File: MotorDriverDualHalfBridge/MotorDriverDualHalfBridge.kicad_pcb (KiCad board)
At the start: 2 copper layers, 41 parts, among them J1 Battery Terminal +, J2 Battery Terminal -, J3 Motor Battery Connection, J4 Motor Load Connection, J5 Conn_01x02_Male, J6 Conn_01x02_Male, K1 G8PM, Q1 IAUA250N04S6N005, Q2 IAUA250N04S6N005, Q3 Q_NMOS_DGS, U1 2ED21824S06J, U2 TLI4871

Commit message: PCB V0.1
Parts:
- added C14: 100uF, Capacitor_SMD:CP_Elec_10x14.3, F.Cu at (171.0, 76.2)
- added C16: 100uF, Capacitor_SMD:CP_Elec_6.3x5.4_Nichicon, F.Cu at (190.1, 94.7)
- added C17: 100uF, Capacitor_SMD:CP_Elec_6.3x5.4_Nichicon, F.Cu at (182.8, 94.7)
- added C18: 100uF, Capacitor_SMD:CP_Elec_6.3x5.4_Nichicon, F.Cu at (175.6, 94.7)
- added C19: 100uF, Capacitor_SMD:CP_Elec_6.3x5.4_Nichicon, F.Cu at (118.2, 100.6)
- added C20: 100uF, Capacitor_SMD:CP_Elec_6.3x5.4_Nichicon, F.Cu at (118.3, 114.4)
- added HS1: Heatsink_Pad, Library:HSB25-282810, F.Cu at (155.3, 105.5)
- added J10: RJ45_LED_Shielded, Connector_RJ:RJ45_Amphenol_RJHSE538X, F.Cu at (113.6, 87.4)
- added J7: Conn_01x06_Pin, Connector_PinHeader_1.27mm:PinHeader_1x06_P1.27mm_Vertical, F.Cu at (112.6, 72.3)
- added NT1: NetTie_2, NetTie:NetTie-2_SMD_Pad2.0mm, F.Cu at (165.8, 62.2)
- C10, C11, C12, R6, R7: moved to B.Cu
- C13, C6: footprint Capacitor_SMD:CP_Elec_5x4.4 -> Capacitor_SMD:CP_Elec_10x14.3
- C4, R4: moved to F.Cu
- F1: footprint Fuse:Fuseholder_Clip-5x20mm_Bel_FC-203-22_Lateral_P17.80x5.00mm_D1.17mm_Horizontal -> Fuse:Fuseholder_Blade_Mini_Keystone_3568
- J5, J6: value Conn_01x02_Male -> Conn_01x04; footprint Connector_PinHeader_1.27mm:PinHeader_1x02_P1.27mm_Vertical -> Connector_JST:JST_EH_B4B-EH-A_1x04_P2.50mm_Vertical
- Q1, Q2: footprint IFX-PG-HSOF-5-1-V:IFX-PG-HSOF-5-1-V -> Library:IAUA250N04S6N005AUMA1
- moved J2 144.0 mm to (162.6, 56.8)
- moved R10 120.3 mm to (107.3, 65.5), turned to 90 degrees
- moved R9 120.0 mm to (109.0, 65.5), turned to -90 degrees
- moved C6 116.1 mm to (126.5, 53.8), turned to 90 degrees
- moved C12 114.8 mm to (109.2, 69.3), turned to 90 degrees
- moved J1 114.4 mm to (142.6, 56.8)
- moved C9 113.7 mm to (112.2, 65.5), turned to 90 degrees
- moved C11 113.3 mm to (107.7, 69.3), turned to 90 degrees
- moved C8 112.3 mm to (110.5, 65.5), turned to 90 degrees
- moved C10 111.9 mm to (106.0, 69.3), turned to 90 degrees
- moved R7 109.8 mm to (112.5, 69.3), turned to -90 degrees
- moved R6 108.3 mm to (110.8, 69.3), turned to -90 degrees
- moved F1 105.4 mm to (137.9, 48.8)
- moved U2 104.5 mm to (127.0, 67.3)
- moved C7 101.8 mm to (124.0, 73.3), turned to 0 degrees
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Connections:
- net Net-(Q1-Pad5) renamed /V_{GH}
- net Net-(Q2-Pad5) renamed /V_{GL}
- C5 pad 2: GND -> GNDPWR
- J5 pad 1: H_{IN} -> +3.3V
- J5 pad 2: L_{IN} -> +3.3V
- J6 pad 1: VCC -> +12V
- J6 pad 2: GND -> +12V
- Q2 pad 1: GND -> GNDPWR
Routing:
- net OCD_{1}: track 0.00 -> 106.4 mm, vias 0 -> 1
- net V_{REF}: track 0.00 -> 59.8 mm
- net OCD_{2}: track 0.00 -> 52.2 mm
- net +12V: track 0.00 -> 52.0 mm, vias 0 -> 3
- net A_{OUT}: track 0.00 -> 51.3 mm
- net /V_{GL}: track 0.00 -> 15.6 mm
- net GND: track 0.00 -> 14.8 mm
- net L_{IN}: track 0.00 -> 11.4 mm
- net H_{IN}: track 0.00 -> 11.3 mm
- net /V_{GH}: track 14.3 -> 24.7 mm
- net Net-(D1-A2): track 0.00 -> 6.96 mm
- net Net-(U1-LO): track 24.4 -> 18.6 mm
- net Net-(C4-Pad1): track 0.00 -> 5.62 mm
- net Net-(U1-HO): track 23.9 -> 18.6 mm
- net Net-(Q3-D): track 0.00 -> 3.94 mm
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- added copper zone on B.Cu, net +12V
- added copper zone on F.Cu, net +12V
- added copper zone on B.Cu, net +3.3V
- added copper zone on F.Cu, net +3.3V
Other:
- board outline added: 90 x 90 mm
- board text added: "12V"
- board text added: "3.3V"
- board text added: "A_{OUT}"
- board text added: "BATTERY+"
- board text added: "BATTERY-"
- board text added: "COM PORT"
- board text added: "Current Sensor"
- board text added: "Designed by M.Kritikakis"
- board text added: "FUSE"
- board text added: "GND"
- board text added: "H_{IN}"
- board text added: "Heatsink"
- board text added: "L_{IN}"
- board text added: "MOTOR+"
- board text added: "MOTOR-"
- board text added: "OCD_{1}"
- board text added: "OCD_{2}"
- board text added: "PWR"
- board text added: "SYM"
- board text added: "Short these two terminals to witness an"
- board text added: "Switching MOSFETS"
- board text added: "TUCer"
- board text added: "V_{REF}"
- board text added: "once in a lifetime event"

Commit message: Updated Schematic
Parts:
- removed C14: 100uF, Capacitor_SMD:CP_Elec_10x14.3
- removed D1: D_TVS, Diode_SMD:D_SMF
- removed J10: RJ45_LED_Shielded, Connector_RJ:RJ45_Amphenol_RJHSE538X
- removed K1: G8PM, Library:G8PM1AW7RDC12
- removed Q3: Q_NMOS_DGS, Package_TO_SOT_THT:TO-220F-3_Vertical
- removed R8: 120Ω, Resistor_SMD:R_0603_1608Metric_Pad0.98x0.95mm_HandSolder
- added J11: Conn_01x03, Library:MOLEX_2078430003_L1NK_250_3-PIN, F.Cu at (117.5, 83.2)
- added J8: Conn_01x03, Library:MOLEX_2078430003_L1NK_250_3-PIN, F.Cu at (117.5, 70.5)
- C8, C9, R10, R9: moved to B.Cu
- J5, J6: footprint Connector_JST:JST_EH_B4B-EH-A_1x04_P2.50mm_Vertical -> Library:MOLEX_2078430004_L1NK_250_4-PIN
- J7: value Conn_01x06_Pin -> Conn_01x03; footprint Connector_PinHeader_1.27mm:PinHeader_1x06_P1.27mm_Vertical -> Library:MOLEX_2078430003_L1NK_250_3-PIN
- U2: footprint Library:PG-TISON-8 -> Library:TLI4971A120T5E0001XUMA1
- moved R10 28.0 mm to (117.6, 91.6), turned to 0 degrees
- moved R9 26.0 mm to (117.6, 90.0), turned to 180 degrees
- moved C13 23.4 mm to (137.8, 68.6), turned to -90 degrees
- moved C12 20.8 mm to (117.6, 88.4), turned to 0 degrees
- moved C11 20.1 mm to (117.6, 86.8), turned to 0 degrees
- moved C10 19.0 mm to (117.6, 84.3), turned to 0 degrees
- moved J7 15.2 mm to (117.5, 57.9)
- moved R6 12.4 mm to (117.6, 58.9), turned to 180 degrees
- moved C8 10.7 mm to (117.6, 57.4), turned to 0 degrees
- moved R7 9.38 mm to (117.6, 61.5), turned to 180 degrees
- moved C9 6.00 mm to (117.6, 63.0), turned to 0 degrees
- moved C20 2.22 mm to (118.7, 116.6)
- moved NT1 1.76 mm to (167.0, 63.5), turned to 90 degrees
- moved J6 1.45 mm to (108.0, 119.4)
- moved C19 1.35 mm to (118.7, 101.9)
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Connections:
- J7 pad 1: H_{IN} -> OCD_{1}
- J7 pad 2: L_{IN} -> OCD_{2}
- J7 pad 3: OCD_{1} -> GND
- U2 pad 7: Net-(U2-IP-) -> +BATT
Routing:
- net OCD_{1}: track 106.4 -> 7.19 mm, vias 1 -> 0
- net +12V: track 52.0 -> 2.13 mm
- net V_{REF}: track 59.8 -> 10.4 mm
- net A_{OUT}: track 51.3 -> 5.62 mm
- net OCD_{2}: track 52.2 -> 7.13 mm
- net L_{IN}: track 11.4 -> 50.8 mm
- net H_{IN}: track 11.3 -> 50.2 mm
- net /LOAD: track 2.41 -> 24.9 mm
- net Net-(D1-A2): track 6.96 -> 0.00 mm
- net Net-(Q3-D): track 3.94 -> 0.00 mm
- removed copper zone on B.Cu, net +3.3V
- removed copper zone on F.Cu, net Net-(U2-IP-)
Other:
- board text added: "COM PORTS"
- board text removed: "COM PORT"

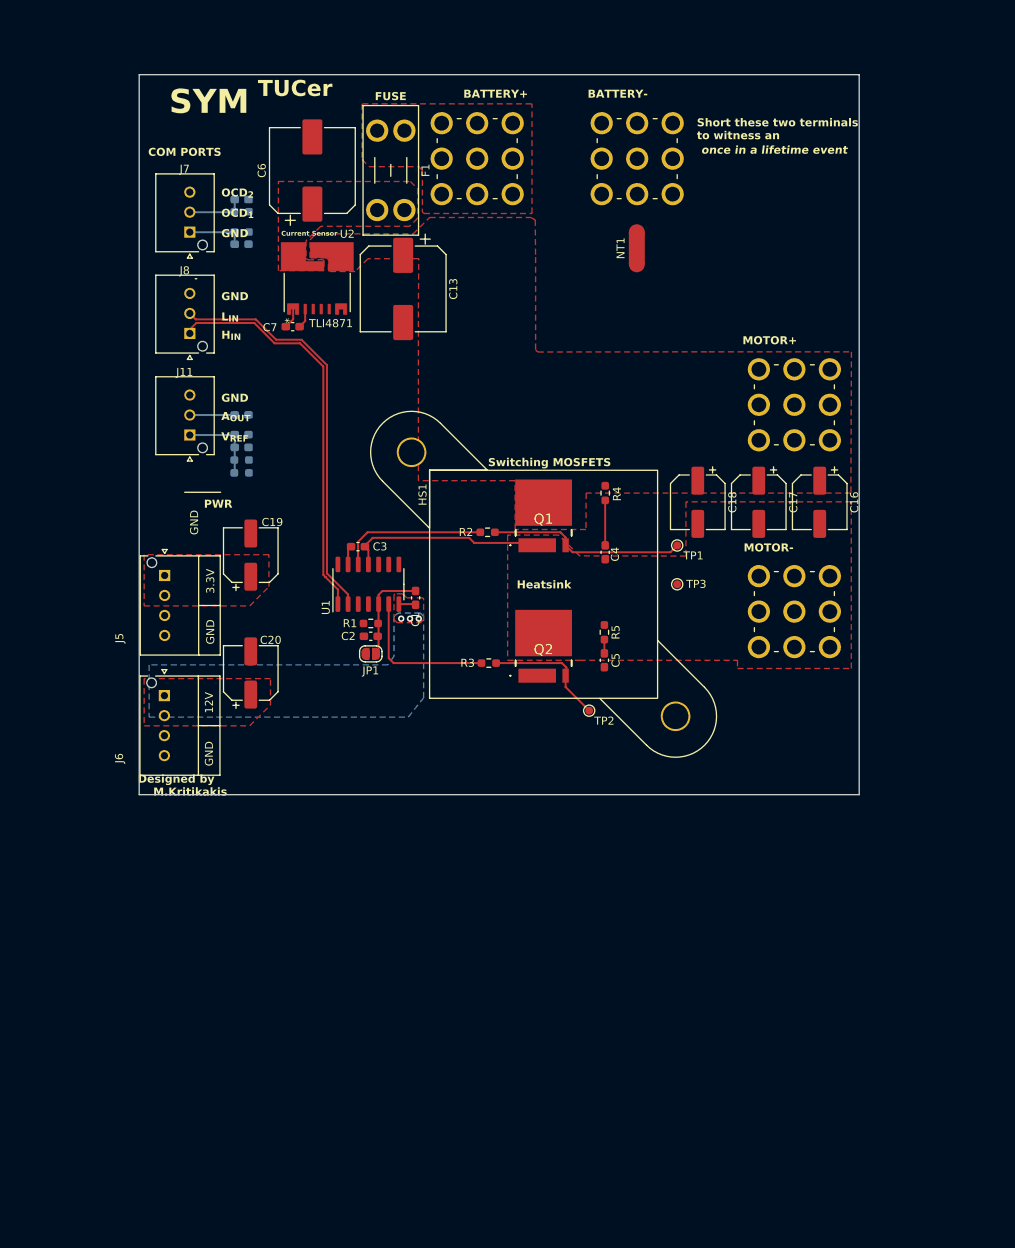
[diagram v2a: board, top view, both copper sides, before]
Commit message: Updated Motor Driver Dual Half Bridge
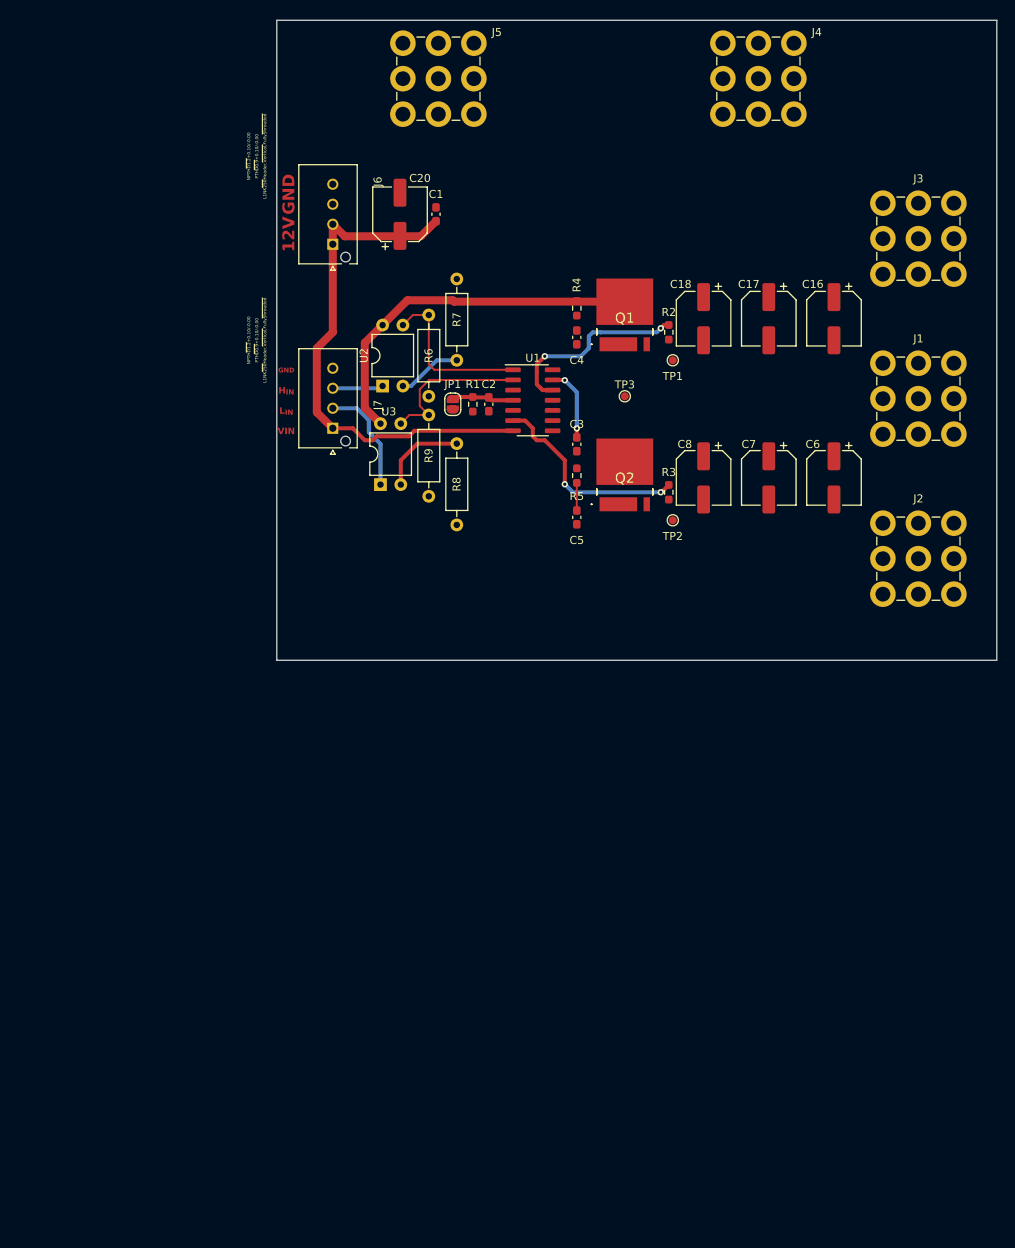
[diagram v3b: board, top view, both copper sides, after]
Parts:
- removed C10, C11, C9: 6.8nF, Capacitor_SMD:C_0603_1608Metric_Pad1.08x0.95mm_HandSolder
- removed C12: 220nF, Capacitor_SMD:C_0603_1608Metric_Pad1.08x0.95mm_HandSolder
- removed C13: 100uF, Capacitor_SMD:CP_Elec_10x14.3
- removed C19: 100uF, Capacitor_SMD:CP_Elec_6.3x5.4_Nichicon
- removed F1: 45A, Fuse:Fuseholder_Blade_Mini_Keystone_3568
- removed HS1: Heatsink_Pad, Library:HSB25-282810
- removed J11, J8: Conn_01x03, Library:MOLEX_2078430003_L1NK_250_3-PIN
- removed NT1: NetTie_2, NetTie:NetTie-2_SMD_Pad2.0mm
- removed R10: 10k, Resistor_SMD:R_0603_1608Metric_Pad0.98x0.95mm_HandSolder
- added R8: R_{DT}, Resistor_THT:R_Axial_DIN0207_L6.3mm_D2.5mm_P10.16mm_Horizontal, F.Cu at (144.5, 87.9)
- added U3: EL817, Package_DIP:DIP-4_W7.62mm, F.Cu at (135.0, 93.0)
- C6: footprint Capacitor_SMD:CP_Elec_10x14.3 -> Capacitor_SMD:CP_Elec_6.3x5.4_Nichicon
- C7: value 220nF -> 100uF; footprint Capacitor_SMD:C_0603_1608Metric_Pad1.08x0.95mm_HandSolder -> Capacitor_SMD:CP_Elec_6.3x5.4_Nichicon
- C8: value 6.8nF -> 100uF; footprint Capacitor_SMD:C_0603_1608Metric_Pad1.08x0.95mm_HandSolder -> Capacitor_SMD:CP_Elec_6.3x5.4_Nichicon; moved to F.Cu
- J1: value Battery Terminal + -> Motor Mid Connection; footprint Library:74651195R -> TerminalBlock_Wuerth:Wuerth_REDCUBE-THR_WP-THRBU_74650194_THR
- J2: value Battery Terminal - -> Motor Low Connection; footprint Library:74651195R -> TerminalBlock_Wuerth:Wuerth_REDCUBE-THR_WP-THRBU_74650194_THR
- J3: value Motor Battery Connection -> Motor Upper Connection; footprint Library:74651195R -> TerminalBlock_Wuerth:Wuerth_REDCUBE-THR_WP-THRBU_74650194_THR
- J4: value Motor Load Connection -> Batt+; footprint Library:74651195R -> TerminalBlock_Wuerth:Wuerth_REDCUBE-THR_WP-THRBU_74650194_THR
- J5: value Conn_01x04 -> Batt-; footprint Library:MOLEX_2078430004_L1NK_250_4-PIN -> TerminalBlock_Wuerth:Wuerth_REDCUBE-THR_WP-THRBU_74650194_THR
- J7: value Conn_01x03 -> Conn_01x04; footprint Library:MOLEX_2078430003_L1NK_250_3-PIN -> Library:MOLEX_2078430004_L1NK_250_4-PIN
- R6, R7: value 4.7kΩ -> R_{DT}; footprint Resistor_SMD:R_0603_1608Metric_Pad0.98x0.95mm_HandSolder -> Resistor_THT:R_Axial_DIN0207_L6.3mm_D2.5mm_P10.16mm_Horizontal; moved to F.Cu
- R9: value 10k -> R_{DT}; footprint Resistor_SMD:R_0603_1608Metric_Pad0.98x0.95mm_HandSolder -> Resistor_THT:R_Axial_DIN0207_L6.3mm_D2.5mm_P10.16mm_Horizontal; moved to F.Cu
- U2: value TLI4871 -> EL817; footprint Library:TLI4971A120T5E0001XUMA1 -> Package_DIP:DIP-4_W7.62mm
- moved C6 75.7 mm to (191.7, 92.2), turned to -90 degrees
- moved J4 71.6 mm to (182.2, 42.3), turned to 0 degrees
- moved J5 70.9 mm to (142.2, 42.3), turned to 0 degrees
- moved C8 67.4 mm to (175.3, 92.2), turned to -90 degrees
- moved J1 64.8 mm to (202.2, 82.3)
- moved C7 62.4 mm to (183.5, 92.2), turned to -90 degrees
- moved J2 60.3 mm to (202.2, 102.3)
- moved C20 60.3 mm to (137.4, 59.2)
- moved J6 60.2 mm to (129.0, 63.0), turned to -90 degrees
- moved C1 48.0 mm to (141.9, 59.2)
- moved R2 33.7 mm to (171.0, 74.0), turned to -90 degrees
- moved JP1 32.8 mm to (144.0, 83.0), turned to 90 degrees
- moved C2 32.5 mm to (148.5, 83.0), turned to -90 degrees
- moved R7 31.3 mm to (144.5, 77.5), turned to 90 degrees
- moved R3 31.0 mm to (171.0, 94.0), turned to -90 degrees
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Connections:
- C6 pad 1: Net-(U2-IP+) -> /LOAD
- C7 pad 1: +3.3V -> /LOAD
- C7 pad 2: GND -> GNDPWR
- C8 pad 1: OCD_{2} -> /LOAD
- C8 pad 2: GND -> GNDPWR
- J1 pad 1: Net-(J1-Pin_1) -> /LOAD
- J4 pad 1: /LOAD -> +BATT
- J5 pad 1: +3.3V -> GNDPWR
- J7 pad 1: OCD_{1} -> +12V
- J7 pad 2: OCD_{2} -> L_{IN}
- J7 pad 3: GND -> H_{IN}
- R6 pad 1: +3.3V -> H_{IN}_{_ISO}
- R6 pad 2: OCD_{2} -> GNDPWR
- R7 pad 1: +3.3V -> Net-(R7-Pad1)
- R7 pad 2: OCD_{1} -> GND
- R9 pad 1: +3.3V -> L_{IN}_{_ISO}
- R9 pad 2: V_{REF} -> GNDPWR
- U1 pad 1: H_{IN} -> H_{IN}_{_ISO}
- U1 pad 2: L_{IN} -> L_{IN}_{_ISO}
- U2 pad 1: +3.3V -> H_{IN}
- U2 pad 2: GND -> Net-(R7-Pad1)
- U2 pad 3: V_{REF} -> H_{IN}_{_ISO}
- U2 pad 4: A_{OUT} -> +BATT
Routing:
- net +12V: track 2.13 -> 65.1 mm, vias 3 -> 0
- net +BATT: track 0.00 -> 45.7 mm
- net H_{IN}: track 50.2 -> 6.34 mm
- net L_{IN}: track 50.8 -> 13.8 mm
- net /LOAD: track 24.9 -> 0.00 mm
- net /V_{GH}: track 24.7 -> 0.00 mm
- net H_{IN}_{_ISO}: track 0.00 -> 20.7 mm
- net L_{IN}_{_ISO}: track 0.00 -> 19.8 mm
- net /V_{GL}: track 15.6 -> 0.00 mm
- net GND: track 14.8 -> 0.00 mm
- net Net-(R8-Pad1): track 0.00 -> 10.9 mm
- net V_{REF}: track 10.4 -> 0.00 mm
- net Net-(R7-Pad1): track 0.00 -> 8.07 mm
- net Net-(JP1-B): track 0.00 -> 7.80 mm
- net Net-(U1-LO): track 18.6 -> 26.0 mm, vias 0 -> 2
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- removed copper zone on B.Cu, net +12V
- removed copper zone on F.Cu, net +12V
- removed copper zone on F.Cu, net +3.3V
- removed copper zone on F.Cu, net +BATT
- removed copper zone on F.Cu, net /LOAD
- removed copper zone on F.Cu, net Net-(J1-Pin_1)
- removed copper zone on F.Cu, net Net-(U2-IP+)
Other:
- board size 90 x 90 mm -> 90 x 80 mm
- board text added: "VIN"
- board text removed: "3.3V"
- board text removed: "A_{OUT}"
- board text removed: "BATTERY+"
- board text removed: "BATTERY-"
- board text removed: "COM PORTS"
- board text removed: "Current Sensor"
- board text removed: "Designed by M.Kritikakis"
- board text removed: "FUSE"
- board text removed: "Heatsink"
- board text removed: "MOTOR+"
- board text removed: "MOTOR-"
- board text removed: "OCD_{1}"
- board text removed: "OCD_{2}"
- board text removed: "PWR"
- board text removed: "SYM"
- board text removed: "Short these two terminals to witness an"
- board text removed: "Switching MOSFETS"
- board text removed: "TUCer"
- board text removed: "V_{REF}"
- board text removed: "once in a lifetime event"

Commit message: Motor Driver V1.0
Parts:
- removed C6: 100uF, Capacitor_SMD:CP_Elec_6.3x5.4_Nichicon
- added Ce1: 100nF, Capacitor_SMD:CP_Elec_6.3x5.4_Nichicon, F.Cu at (191.7, 92.2)
- added H1: MountingHole_Pad, MountingHole:MountingHole_2.5mm_Pad, F.Cu at (126.0, 39.0)
- added H2: MountingHole_Pad, MountingHole:MountingHole_2.5mm_Pad, F.Cu at (208.0, 39.0)
- added H3: MountingHole_Pad, MountingHole:MountingHole_2.5mm_Pad, F.Cu at (126.0, 111.0)
- added H4: MountingHole_Pad, MountingHole:MountingHole_2.5mm_Pad, F.Cu at (182.0, 111.0)
- added H5: MountingHole_Pad, MountingHole:MountingHole_2.5mm_Pad, F.Cu at (182.0, 59.0)
- C16, C17, C18, C7, C8: value 100uF -> 100nF
- C4, C5: footprint Capacitor_SMD:C_0603_1608Metric_Pad1.08x0.95mm_HandSolder -> Capacitor_SMD:C_0805_2012Metric_Pad1.18x1.45mm_HandSolder
- J1: value Motor Mid Connection -> Motor Middle Connection; footprint TerminalBlock_Wuerth:Wuerth_REDCUBE-THR_WP-THRBU_74650194_THR -> Library:M5 Screw Terminal
- J2: value Motor Low Connection -> Motor Bottom Connection; footprint TerminalBlock_Wuerth:Wuerth_REDCUBE-THR_WP-THRBU_74650194_THR -> Library:M5 Screw Terminal
- J3, J4, J5: footprint TerminalBlock_Wuerth:Wuerth_REDCUBE-THR_WP-THRBU_74650194_THR -> Library:M5 Screw Terminal
- R2, R3, R4, R5: footprint Resistor_SMD:R_0603_1608Metric_Pad0.98x0.95mm_HandSolder -> Resistor_SMD:R_0805_2012Metric_Pad1.20x1.40mm_HandSolder
- moved R6 8.82 mm to (144.1, 80.1), turned to 90 degrees
- moved J4 8.00 mm to (182.2, 50.3)
- moved J5 8.00 mm to (142.2, 50.3)
- moved R8 7.47 mm to (140.9, 94.5), turned to 90 degrees
- moved R7 5.83 mm to (140.9, 82.1)
- moved J1 5.66 mm to (198.2, 86.3)
- moved J2 5.66 mm to (198.2, 106.3)
- moved J3 5.66 mm to (198.2, 66.3)
- moved R9 3.47 mm to (144.1, 85.9)
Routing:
- net Earth_Clean: track 0.00 -> 78.8 mm, vias 0 -> 16
- net GND: track 0.00 -> 63.1 mm
- net /LOAD: track 0.00 -> 9.23 mm
- net Net-(R8-Pad1): track 10.9 -> 3.99 mm
- net Net-(R7-Pad1): track 8.07 -> 3.70 mm
- net +BATT: track 45.7 -> 47.6 mm
- net H_{IN}_{_ISO}: track 20.7 -> 19.7 mm
- net +12V: track 65.1 -> 65.9 mm
- net L_{IN}_{_ISO}: track 19.8 -> 19.5 mm, vias 0 -> 1
- net GNDPWR: vias 0 -> 73
- added copper zone on F.Cu, net +12V
- added copper zone on B.Cu, net +BATT
- added copper zone on F.Cu, net +BATT
- added copper zone on F.Cu, net /LOAD
- added copper zone on F.Cu, net /V_{GH}
- added copper zone on F.Cu, net /V_{GL}
- added copper zone on B.Cu, net Earth_Clean
- added copper zone on F.Cu, net Earth_Clean
- added copper zone on F.Cu, net GND
- added copper zone on B.Cu, net GNDPWR
- added copper zone on F.Cu, net GNDPWR
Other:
- board text added: "M"
- board text added: "M+"
- board text added: "M-"
- board text added: "SYM"

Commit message: Motor Driver V1.0
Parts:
- moved C16 0.40 mm to (192.1, 72.3)
- moved C17 0.40 mm to (183.9, 72.3)
- moved C18 0.40 mm to (175.8, 72.3)
- moved C7 0.40 mm to (183.9, 92.2)
- moved C8 0.40 mm to (175.8, 92.2)
- moved Ce1 0.40 mm to (192.1, 92.2)
- moved C4 0.26 mm to (159.5, 74.9)
- moved R2 0.10 mm to (171.1, 74.0)
- moved R3 0.10 mm to (171.1, 94.0)
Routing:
- net Net-(C4-Pad1): track 0.00 -> 1.86 mm
